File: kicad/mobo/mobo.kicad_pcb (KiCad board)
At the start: 4 copper layers, 17 x 53.5 mm, 49 parts, among them J1 HRO_TYPE-C-31-M-14, J2 Battery, J3 rgb, J4 columns, J5 Conn_01x10, J6 rows, J7 sensor, Q1 AO3401A, Q2 2N7002, SW1 Battery, SW2 Reset, U1 BQ24075, U2 nRF52840_E73-2G4M08S1C, Y1 32.768 KHz

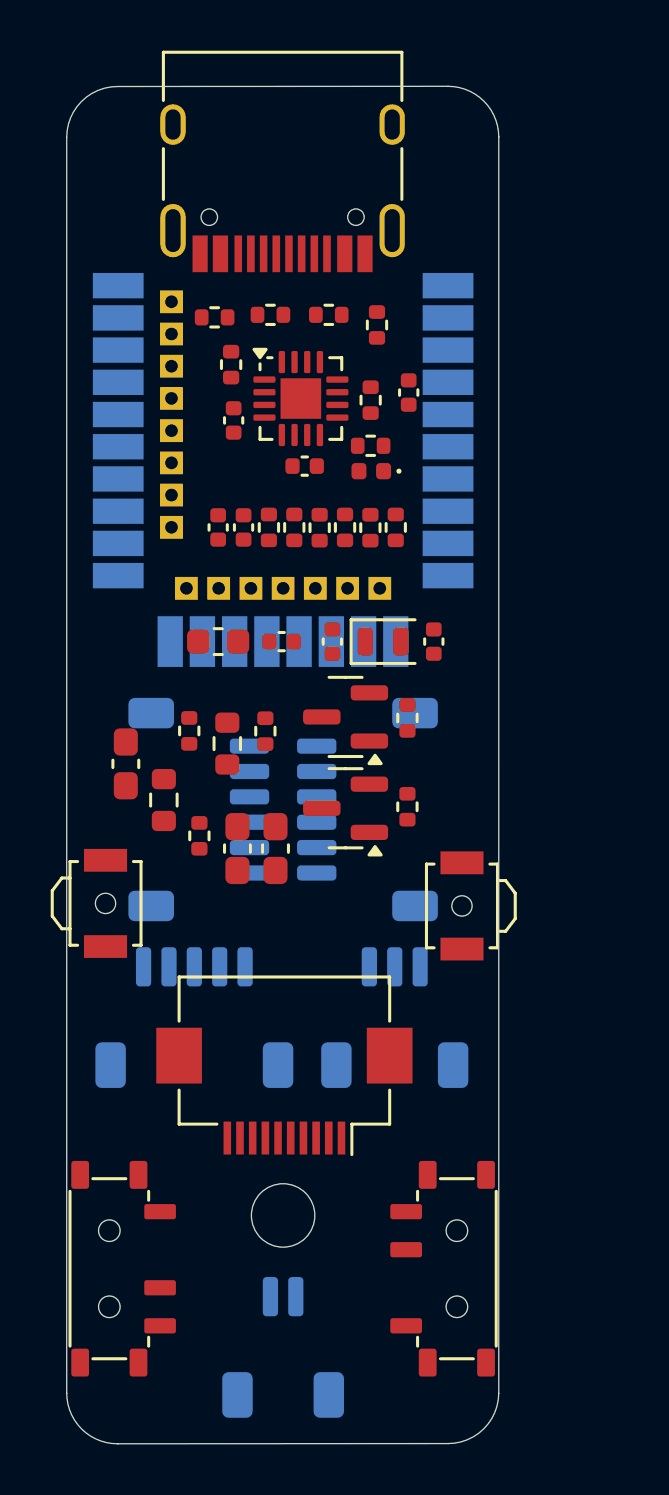
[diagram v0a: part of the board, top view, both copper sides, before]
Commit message: Sub-compacting the components to their target dimensions
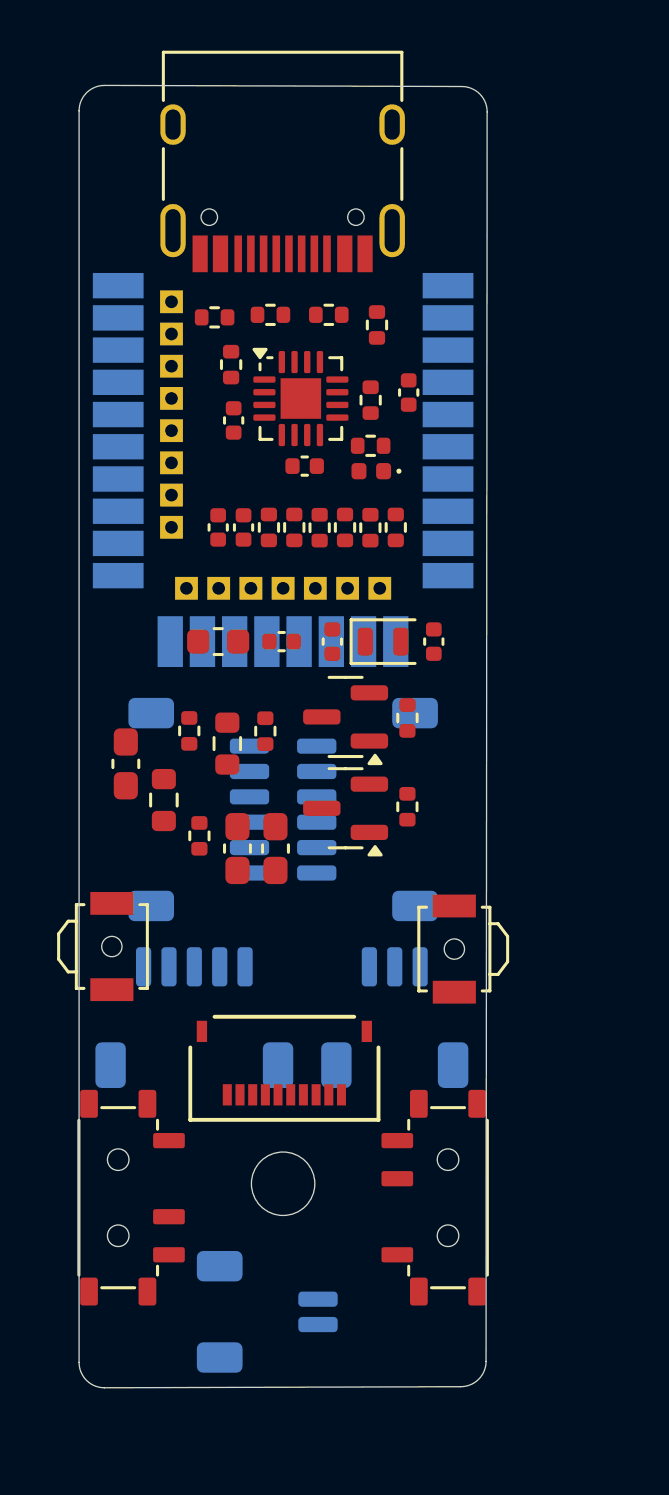
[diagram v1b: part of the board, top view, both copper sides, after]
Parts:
- J5: footprint Connector_FFC-FPC:Hirose_FH12-10S-0.5SH_1x10-1MP_P0.50mm_Horizontal -> Hirose FH34SRJ-10S-0.5SH:CONN10x1_FH34SRJ-10S-0.5SH50_HIR
- moved SW1 2.82 mm to (156.5, 101.3)
- moved SW1 2.82 mm to (143.5, 101.3)
- moved SW2 1.73 mm to (156.8, 91.5)
- moved SW2 1.72 mm to (143.2, 91.4)
- moved J2 1.53 mm to (149.4, 105.8), turned to 90 degrees
- moved J5 0.90 mm to (150.1, 96.2)
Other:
- board size 17 x 53.5 mm -> 16.1 x 51.3 mm

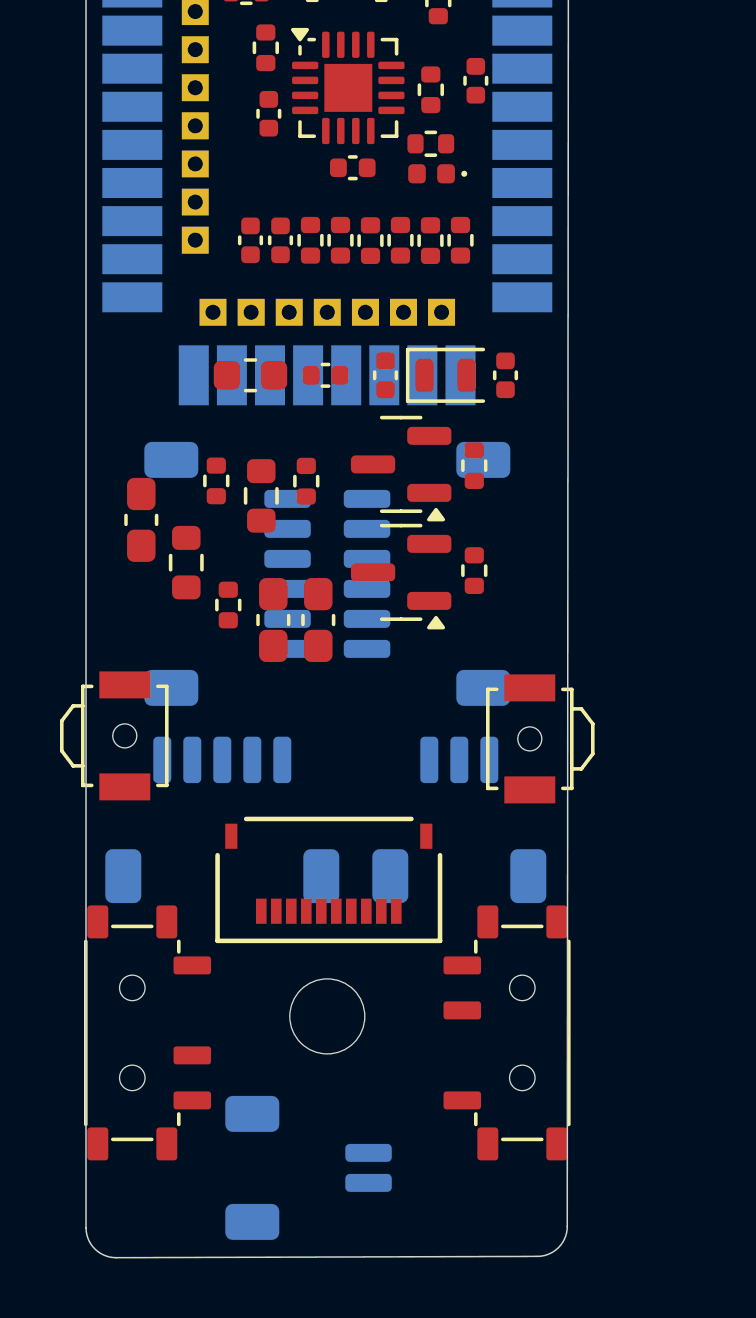
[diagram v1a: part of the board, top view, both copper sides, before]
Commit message: Partially wiring the bottom half
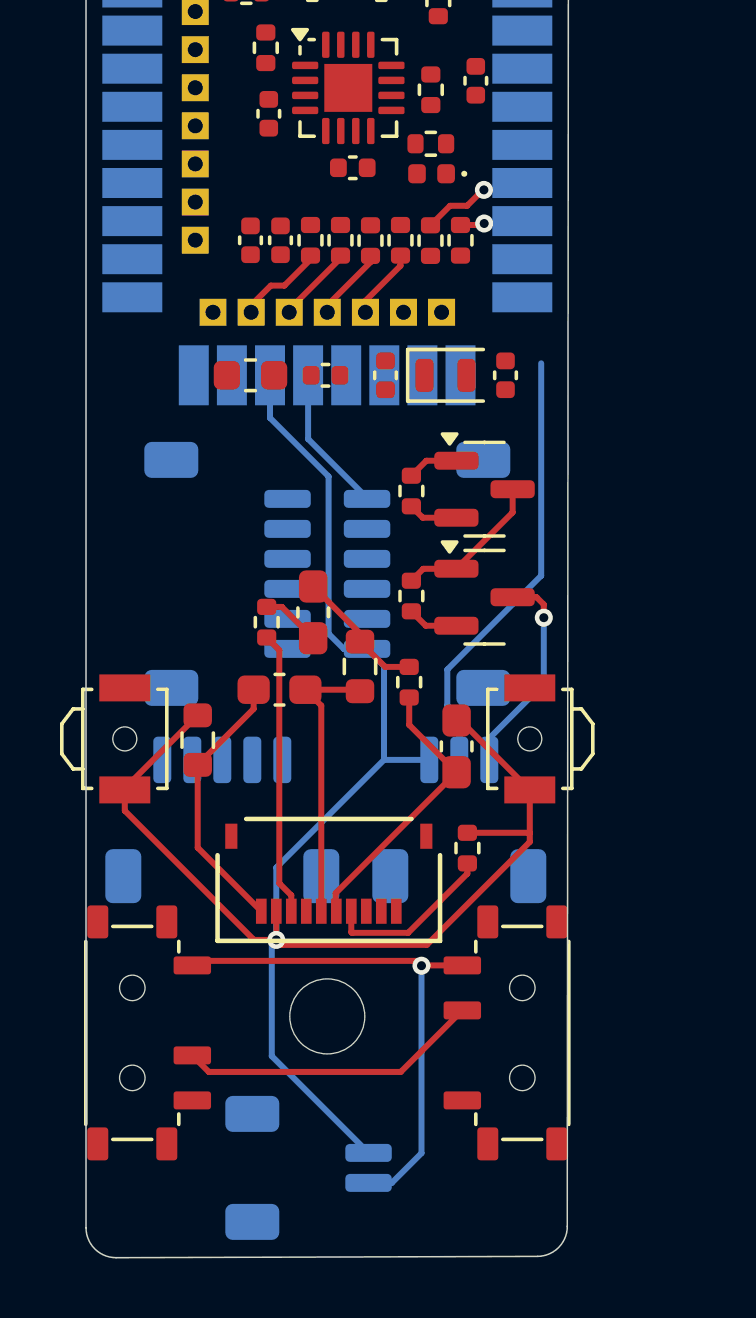
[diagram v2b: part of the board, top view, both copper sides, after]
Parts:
- moved R13 13.4 mm to (154.7, 95.1), turned to 90 degrees
- moved R9 9.29 mm to (152.7, 89.6), turned to -90 degrees
- moved C10 7.30 mm to (148.4, 89.9), turned to 180 degrees
- moved FB1 6.57 mm to (151.1, 89.1), turned to 90 degrees
- moved C7 6.24 mm to (154.3, 91.8), turned to 90 degrees
- moved FB2 5.93 mm to (145.7, 91.5), turned to -90 degrees
- moved Q1 5.23 mm to (155.2, 86.8), turned to 0 degrees
- moved R10 4.83 mm to (152.8, 86.7), turned to 90 degrees
- moved Q2 3.92 mm to (155.2, 83.2), turned to 0 degrees
- moved R18 3.38 mm to (152.8, 83.2), turned to -90 degrees
- moved R12 1.40 mm to (148.0, 87.6), turned to 90 degrees
- moved C8 1.35 mm to (149.5, 87.3)
- moved SW2 0.10 mm to (143.2, 91.5)
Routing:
- net GND: track 0.00 -> 65.1 mm, vias 0 -> 1
- net Net-(J2-Pin_1): track 0.00 -> 17.6 mm, vias 0 -> 1
- net Net-(J3-Pin_2): track 0.00 -> 14.7 mm
- net +BATT: track 0.00 -> 10.1 mm
- net EXTMODE: track 0.00 -> 9.46 mm
- net Net-(J5-Pin_5): track 0.00 -> 9.46 mm
- net VDDA: track 0.00 -> 9.45 mm
- net VDD: track 0.00 -> 9.41 mm
- net GNDA: track 0.00 -> 9.04 mm
- net RGB_PWR: track 0.00 -> 7.07 mm, vias 0 -> 1
- net EXTCOMIN: track 0.00 -> 5.74 mm
- net Net-(Q1-G): track 0.00 -> 5.09 mm
- net RGB_DATA: track 0.00 -> 3.64 mm, vias 0 -> 1
- net SENSOR_IRQ: track 0.00 -> 2.97 mm
- net SENSOR_CLK: track 0.00 -> 2.60 mm
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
